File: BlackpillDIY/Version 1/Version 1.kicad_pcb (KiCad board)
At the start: 2 copper layers, 78 x 39.1 mm, 39 parts, among them J1 Conn_01x08, J2 Conn_01x08, J3 Debug, J4 Left Header, J5 Right Header, J6 Conn_01x05, J7 Conn_01x05, J8 Conn_01x05, J9 Conn_01x08, U1 HT-CT62, U2 STM32F411CCUx, U3 SAM-M8Q, U4 LIS2MDL, Y1 LFXTAL062558Reel, Y2 Crystal_GND24

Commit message: board breaks
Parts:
- moved J8 28.3 mm to (103.3, 50.7)
- moved C13 28.3 mm to (92.9, 53.8)
- moved C14 28.3 mm to (98.5, 54.8)
- moved C15 28.3 mm to (95.7, 58.1)
- moved U4 28.3 mm to (96.0, 54.6)
- moved J7 21.8 mm to (89.2, 36.8)
- moved U3 21.8 mm to (99.3, 31.7)
- moved C11 21.8 mm to (101.2, 22.0)
- moved C12 21.8 mm to (92.5, 22.0)
- moved J6 21.8 mm to (109.5, 36.8)
- moved C4 16.2 mm to (67.7, 21.8)
- moved C5 16.2 mm to (61.5, 21.8)
- moved J2 16.2 mm to (51.9, 41.6)
- moved Y1 16.2 mm to (64.6, 21.8)
- moved C16 16.2 mm to (77.3, 49.4)
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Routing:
- net (no net): vias 0 -> 48
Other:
- board size 78 x 39.1 mm -> 96.5 x 43.2 mm

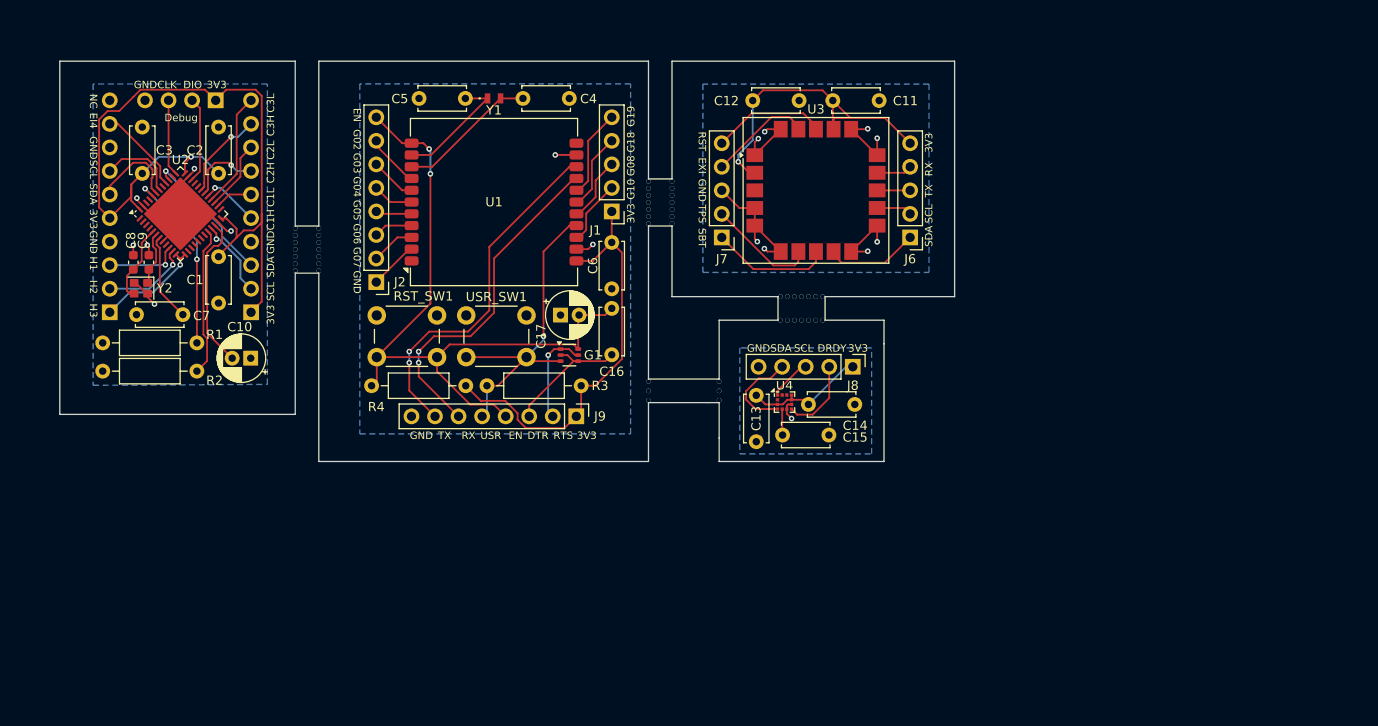
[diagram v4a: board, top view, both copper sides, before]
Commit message: Changed to a single breadboard capable PCB
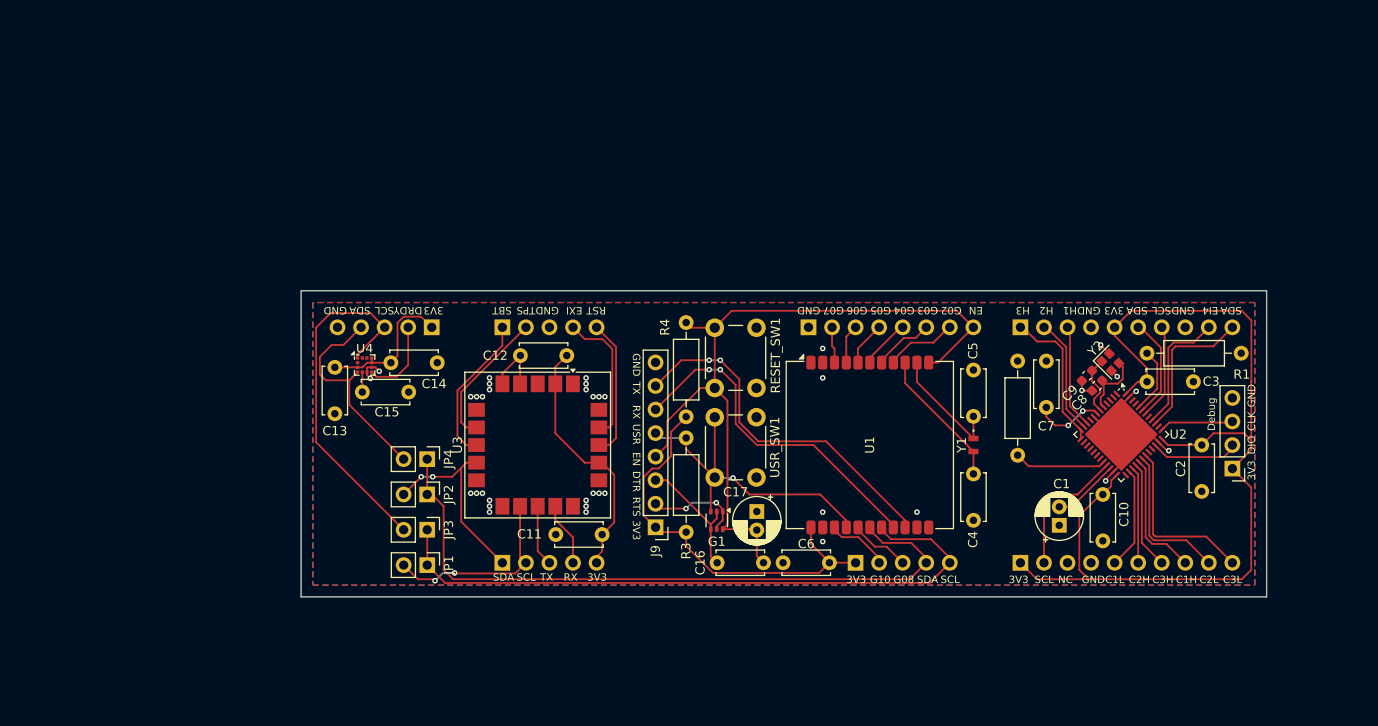
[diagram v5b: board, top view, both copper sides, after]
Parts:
- added G***: LOGO, Symbols:Traccy Logo, B.Cu at (104.3, 58.2)
- added JP1: Jumper_2_Open, Connector_PinHeader_2.54mm:PinHeader_1x02_P2.54mm_Vertical, F.Cu at (57.4, 72.1)
- added JP2: Jumper_2_Open, Connector_PinHeader_2.54mm:PinHeader_1x02_P2.54mm_Vertical, F.Cu at (57.4, 64.5)
- added JP3: Jumper_2_Open, Connector_PinHeader_2.54mm:PinHeader_1x02_P2.54mm_Vertical, F.Cu at (57.4, 68.3)
- added JP4: Jumper_2_Open, Connector_PinHeader_2.54mm:PinHeader_1x02_P2.54mm_Vertical, F.Cu at (57.4, 60.7)
- J1, J2, J6, J7, J8: moved to B.Cu
- J3: moved to F.Cu
- moved R1 122.8 mm to (145.2, 49.3), turned to 180 degrees
- moved J3 116.6 mm to (144.3, 61.7), turned to 180 degrees
- moved C3 110.7 mm to (135.1, 52.4), turned to 0 degrees
- moved C2 110.0 mm to (141.0, 59.2), turned to -90 degrees
- moved Y2 104.9 mm to (131.1, 50.2), turned to -45 degrees
- moved C8 104.8 mm to (129.7, 52.8), turned to 45 degrees
- moved U2 104.2 mm to (132.3, 58.0), turned to -45 degrees
- moved C9 101.9 mm to (128.6, 51.7), turned to 45 degrees
- moved C1 98.8 mm to (130.3, 64.5)
- moved R2 98.7 mm to (121.1, 50.1), turned to -90 degrees
- moved C7 98.3 mm to (124.2, 50.1), turned to -90 degrees
- moved J4 98.2 mm to (121.4, 46.5), turned to -90 degrees
- moved C10 89.1 mm to (125.6, 67.9), turned to 90 degrees
- moved J5 87.3 mm to (121.4, 71.9), turned to -90 degrees
- moved C5 64.6 mm to (116.3, 56.1), turned to 90 degrees
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- renumbered RST_SW1 to RESET_SW1
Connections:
- net /GPIO18 renamed /SDA
- net /GPIO19 renamed /SCL
- C1 pad 2: GND1 -> GND
- C10 pad 1: GND1 -> GND
- C11 pad 2: GND3 -> GND
- C12 pad 2: GND3 -> GND
- C13 pad 2: GND4 -> GND
- C14 pad 2: GND4 -> GND
- C15 pad 2: GND4 -> GND
- C17 pad 1: GND2 -> GND
- C2 pad 2: GND1 -> GND
- C3 pad 2: GND1 -> GND
- C4 pad 2: GND2 -> GND
- C5 pad 2: GND2 -> GND
- C6 pad 2: GND2 -> GND
- C7 pad 1: GND1 -> GND
- C8 pad 1: GND1 -> GND
- C9 pad 1: GND1 -> GND
- J2 pad 1: GND2 -> GND
- J4 pad 10: unconnected-(J4-Pin_10-Pad10) -> I2C2_SDA
- J4 pad 4: GND1 -> GND
- J5 pad 10: TIM1_CH3N -> TIM1_CH3
- J5 pad 3: I2C2_SDA -> unconnected-(J5-Pin_3-Pad3)
- J5 pad 4: GND1 -> GND
- J5 pad 5: TIM1_CH1 -> TIM1_CH1N
- J5 pad 6: TIM1_CH1N -> TIM1_CH2N
- J5 pad 7: TIM1_CH2 -> TIM1_CH3N
- J5 pad 8: TIM1_CH2N -> TIM1_CH1
- J5 pad 9: TIM1_CH3 -> TIM1_CH2
- J7 pad 3: GND3 -> GND
- J8 pad 5: GND4 -> GND
- J9 pad 8: GND2 -> GND
- R1 pad 1: GND1 -> GND
- R2 pad 1: GND1 -> GND
- RESET_SW1 pad 1: GND2 -> GND
- U1 pad 13: GND2 -> GND
- U1 pad 2: GND2 -> GND
- U1 pad 21: GND2 -> GND
- U2 pad 23: GND1 -> GND
- U2 pad 35: GND1 -> GND
- U2 pad 47: GND1 -> GND
- U2 pad 49: GND1 -> GND
- U2 pad 8: GND1 -> GND
- U3 pad 1: GND3 -> GND
- U3 pad 10: GND3 -> GND
- U3 pad 11: GND3 -> GND
- U3 pad 15: GND3 -> GND
- U3 pad 16: GND3 -> GND
- U3 pad 20: GND3 -> GND
- U3 pad 4: GND3 -> GND
- U3 pad 5: GND3 -> GND
- U3 pad 6: GND3 -> GND
- U4 pad 6: GND4 -> GND
- U4 pad 8: GND4 -> GND
- USR_SW1 pad 1: GND2 -> GND
- Y2 pad 2: GND1 -> GND
- Y2 pad 4: GND1 -> GND
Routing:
- net /SDA: track 8.34 -> 74.3 mm
- net /SCL: track 9.61 -> 71.3 mm
- net GND3: track 37.1 -> 0.00 mm, vias 8 -> 0
- net GND: track 0.00 -> 35.7 mm, vias 0 -> 37
- net /SCL2: track 4.58 -> 38.9 mm
- net GND1: track 27.0 -> 0.00 mm, vias 6 -> 0
- net +3.3V1: track 86.4 -> 105.0 mm, vias 1 -> 0
- net /SCL1: track 3.82 -> 21.1 mm, vias 0 -> 2
- net /SDA2: track 9.70 -> 23.3 mm
- net /BOOT0: track 20.1 -> 7.10 mm, vias 2 -> 0
- net /SDA1: track 10.1 -> 21.4 mm, vias 0 -> 2
- net GND2: track 9.56 -> 0.00 mm, vias 2 -> 0
- net /VCAP: track 16.8 -> 7.21 mm
- net TIM1_CH3: track 9.77 -> 18.7 mm, vias 1 -> 0
- net TIM1_CH2: track 8.00 -> 16.3 mm, vias 1 -> 0
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- added copper zone on B.Cu, net GND
- added copper zone on F.Cu, net GND
- removed copper zone on B.Cu, net GND1
- removed copper zone on B.Cu, net GND2
- removed copper zone on B.Cu, net GND3
- removed copper zone on B.Cu, net GND4
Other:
- board size 96.5 x 43.2 mm -> 104.1 x 33 mm
- board text removed: "G18"
- board text removed: "G19"
